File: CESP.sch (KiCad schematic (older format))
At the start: 5 parts

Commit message: First draft of schematic
First draft of having added and connected items in the schematic,
annotated and sized the devices and added a netlist.
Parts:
- removed U?: LTC1594CS, TSSOP14, symbol LTC1594CS
- removed U?: TL074, TSSOP14, symbol TL074
- removed U? (x3): TL074, symbol TL074
- added BT1, BT2: 9V, ~, symbol BATTERY
- added C1, C2, C5: .1µF, ~, symbol C
- added C3, C4: 10µF, ~, symbol CAPAPOL
- added R1: 68K, ~, symbol R
- added R2, R3, R5: 1K, ~, symbol R
- added R4: 10K, ~, symbol R
- added R6: 2K2, ~, symbol R
- added U1: 7555, ~, symbol 7555
- added U2: LM741, symbol LM741
- added U3: 7805, ~, symbol 7805
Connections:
- net labels added: +5V, +9V, -9V, GND
- wire segments 0 -> 47
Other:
- note removed: "NOTE: THIS IS JUST A TEST BOARD\nREMOVE ALL COMPONENTS AND CREATE YOUR OWN\nINCLUDE SCHEMATIC HOOKUPS/NETLIST"

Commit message: Post ERC...
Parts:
- removed BT1, BT2: 9V, ~, symbol BATTERY
- added K1: CONN_3, symbol CONN_3
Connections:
- net labels removed: +5V
- wire segments 47 -> 48
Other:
- moved on the sheet: C1, C2, C3, C4, C5, R1, R2, R3, R4, R5, R6, U1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

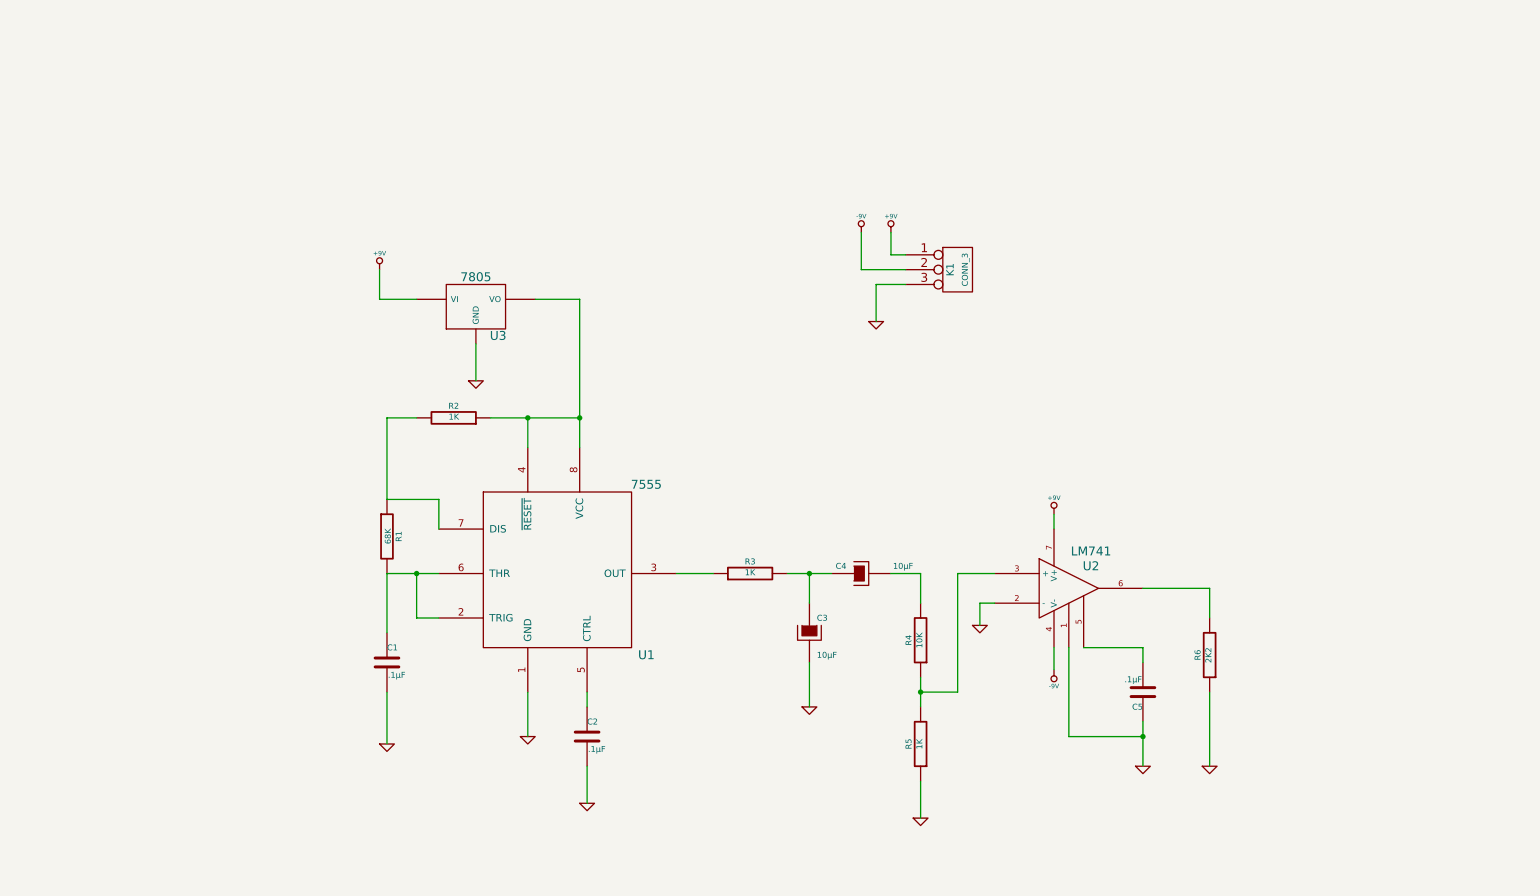
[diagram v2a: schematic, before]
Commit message: First draft of PCB layout
It's a total mess, but I got it to pass ERC, have the 7805 connected,
used a bunch of different foot prints, used vias and successfully beat
my head against the brickwall of KiCad.
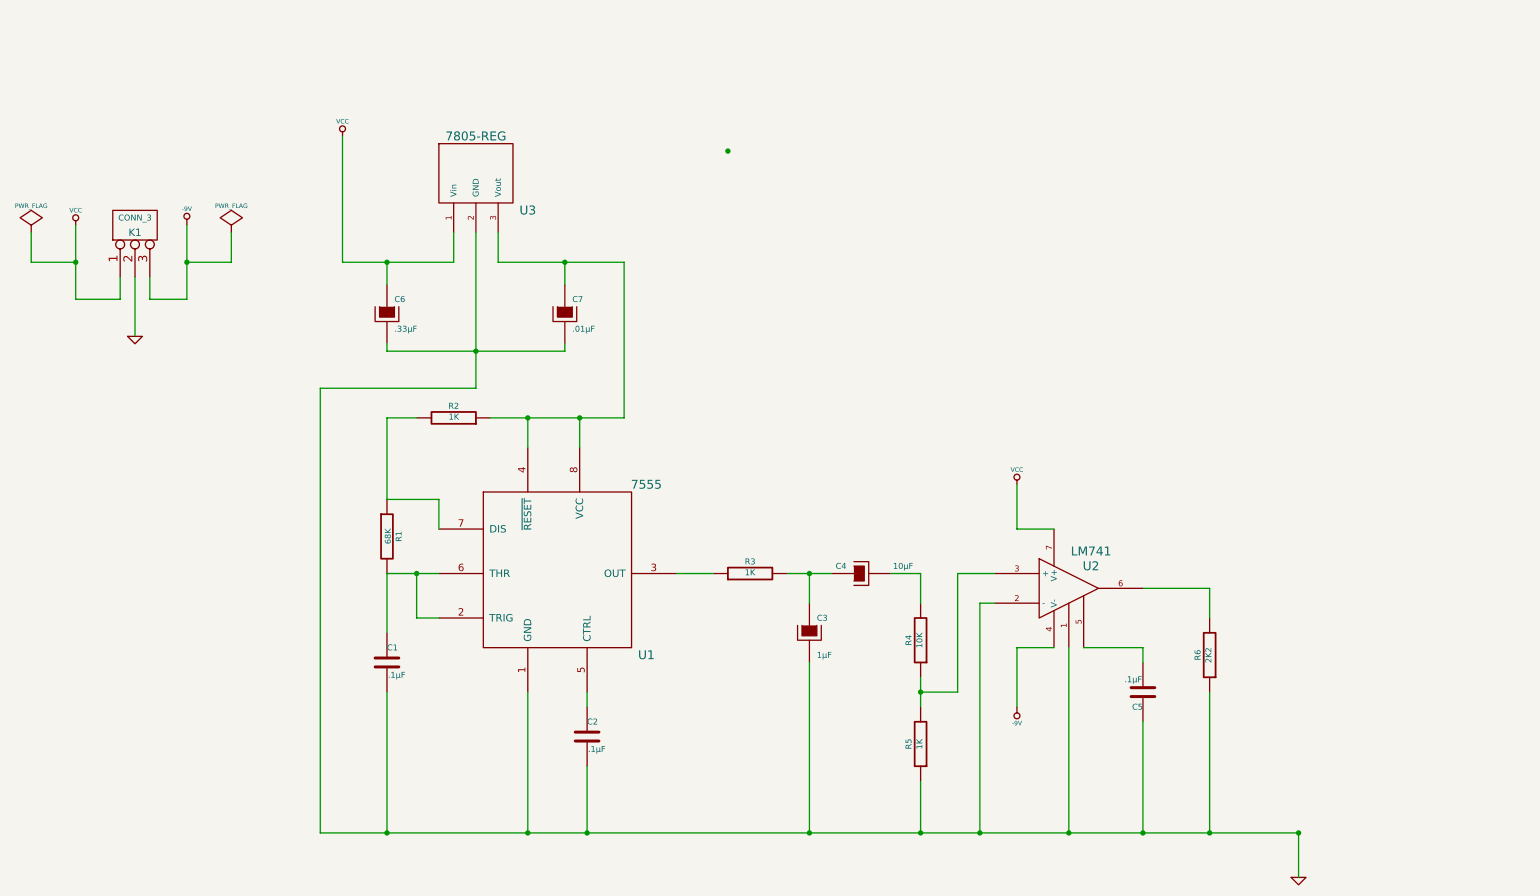
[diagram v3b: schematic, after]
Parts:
- removed U3: 7805, ~, symbol 7805
- added C6: .33µF, ~, symbol CAPAPOL
- added C7: .01µF, ~, symbol CAPAPOL
- added U3: 7805-REG, symbol 7805-REG
- C3: value 10µF -> 1µF
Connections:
- net -9V: now also K1.3 (P3); no longer K1.2 (PM)
- net GND: now also K1.2 (PM), C6.2, C7.2, U3.2 (GND); no longer K1.3 (P3)
- net at R2.1, U1.4 (~RESET), U1.8 (VCC): now also C7.1, U3.3 (Vout)
- net +9V renamed VCC
- net VCC: now also C6.1, U3.1 (Vin)
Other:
- moved on the sheet: K1

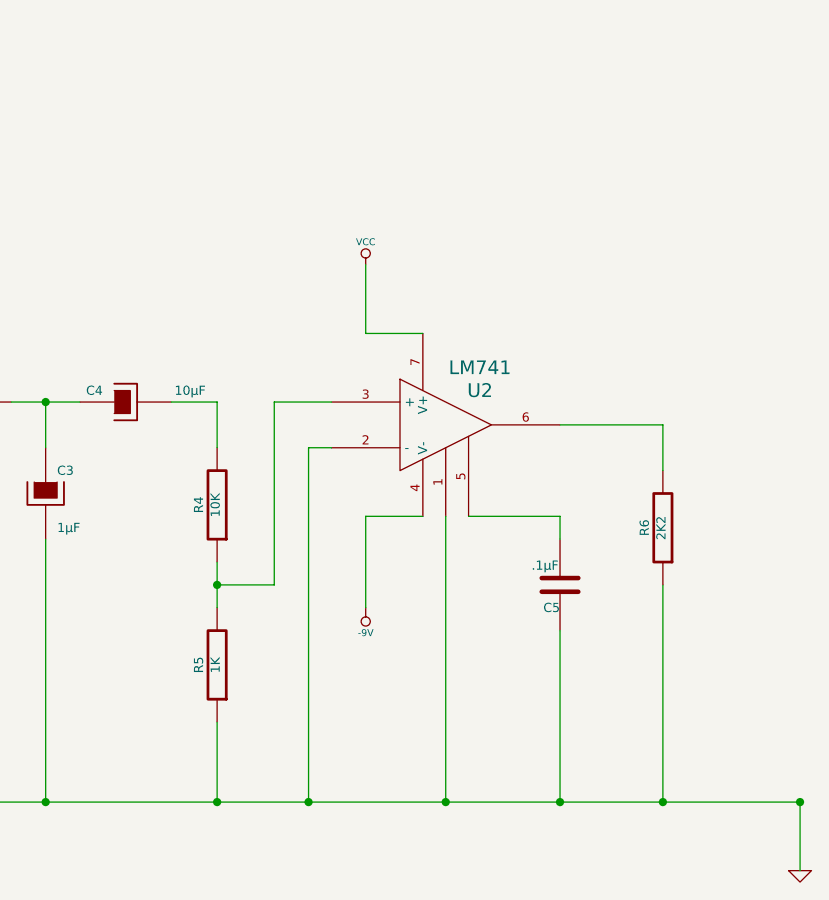
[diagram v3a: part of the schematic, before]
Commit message: Added headers and SPI vs SPI logo...
Headers added to allow customizing the Signal and Feedback resistors.

Headers added to allow measurement with an oscilloscope.

SPI vs. SPI logo from John Lohe added.
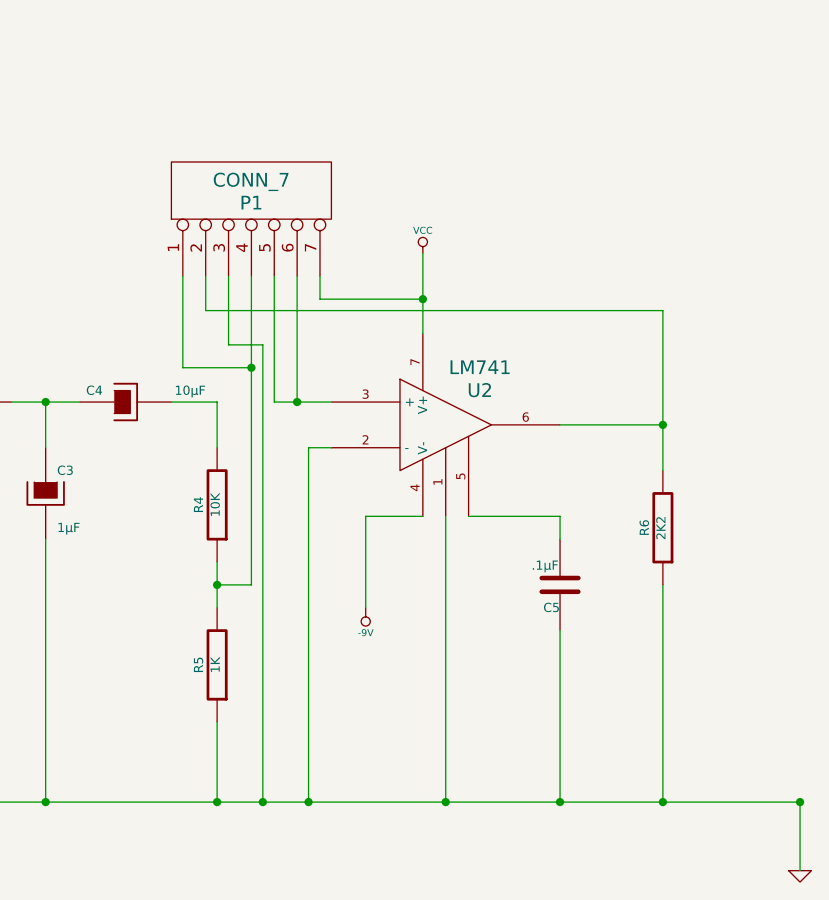
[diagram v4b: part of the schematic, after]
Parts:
- added P1: CONN_7, symbol CONN_7
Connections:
- net GND: now also P1.3 (P3)
- net VCC: now also P1.7 (P7)
- net at R4.1, R5.2: now also P1.1 (P1), P1.4 (P4); no longer U2.3 (+)
- net at R6.2, U2.6: now also P1.2 (P2)
- new net: P1.5 (P5), P1.6 (P6), U2.3 (+)
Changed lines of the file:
@@
 Sheet 1 1
 Title ""
-Date "27 jan 2014"
+Date "28 jan 2014"
 Rev ""
 Comp ""
@@
 Wire Wire Line
 	6800 5100 6800 5300
-Wire Wire Line
-	7300 4400 7050 4400
-Wire Wire Line
-	7050 4400 7050 5200
-Wire Wire Line
-	7050 5200 6800 5200
 Connection ~ 6800 5200
 Wire Wire Line
@@
 	8300 4500 8750 4500
 Wire Wire Line
-	8750 4500 8750 4700
+	8750 4000 8750 4700
 Wire Wire Line
 	4500 3350 4500 3550
@@
 Wire Wire Line
 	7300 4600 7200 4600
-Wire Wire Line
-	7200 4600 7200 6150
 Connection ~ 7200 6150
 $Comp
@@
 	9350 6150 9350 6450
 Wire Wire Line
-	7450 4100 7700 4100
-Wire Wire Line
-	7450 3800 7450 4100
-Wire Wire Line
 	7700 4900 7450 4900
 Wire Wire Line
 	7450 4900 7450 5300
 $Comp
-L VCC #PWR01
+L VCC #PWR1
 U 1 1 52E6ACAC
 P 1100 2050
-F 0 "#PWR01" H 1100 2150 30  0001 C CNN
+F 0 "#PWR1" H 1100 2150 30  0001 C CNN
 F 1 "VCC" H 1100 2150 30  0000 C CNN
 F 2 "" H 1100 2050 60  0000 C CNN
@@
 	1100 2550 1100 2050
 $Comp
-L -9V #PWR02
+L -9V #PWR3
 U 1 1 52E6AD0C
 P 1850 2050
-F 0 "#PWR02" H 1850 2020 20  0001 C CNN
+F 0 "#PWR3" H 1850 2020 20  0001 C CNN
 F 1 "-9V" H 1850 2160 30  0000 C CNN
 F 2 "~" H 1850 2050 60  0000 C CNN
@@
 	1600 2550 1600 2400
 $Comp
-L GND #PWR03
+L GND #PWR2
 U 1 1 52E6AD76
 P 1500 2800
-F 0 "#PWR03" H 1500 2800 30  0001 C CNN
+F 0 "#PWR2" H 1500 2800 30  0001 C CNN
 F 1 "GND" H 1500 2730 30  0001 C CNN
 F 2 "" H 1500 2800 60  0000 C CNN
@@
 	1500 2400 1500 2800
 $Comp
-L VCC #PWR04
+L VCC #PWR4
 U 1 1 52E6ADD6
 P 2900 1450
-F 0 "#PWR04" H 2900 1550 30  0001 C CNN
+F 0 "#PWR4" H 2900 1550 30  0001 C CNN
 F 1 "VCC" H 2900 1550 30  0000 C CNN
 F 2 "" H 2900 1450 60  0000 C CNN
@@
 $EndComp
 $Comp
-L GND #PWR05
+L GND #PWR7
 U 1 1 52E6AE37
 P 9350 6450
-F 0 "#PWR05" H 9350 6450 30  0001 C CNN
+F 0 "#PWR7" H 9350 6450 30  0001 C CNN
 F 1 "GND" H 9350 6380 30  0001 C CNN
 F 2 "" H 9350 6450 60  0000 C CNN
@@
 $EndComp
 $Comp
-L VCC #PWR06
+L VCC #PWR6
 U 1 1 52E6AE98
-P 7450 3800
-F 0 "#PWR06" H 7450 3900 30  0001 C CNN
-F 1 "VCC" H 7450 3900 30  0000 C CNN
-F 2 "" H 7450 3800 60  0000 C CNN
-F 3 "" H 7450 3800 60  0000 C CNN
-	1    7450 3800
-	1    0    0    -1
-$EndComp
-$Comp
-L -9V #PWR07
+P 7700 3750
+F 0 "#PWR6" H 7700 3850 30  0001 C CNN
+F 1 "VCC" H 7700 3850 30  0000 C CNN
+F 2 "" H 7700 3750 60  0000 C CNN
+F 3 "" H 7700 3750 60  0000 C CNN
+	1    7700 3750
+	1    0    0    -1
+$EndComp
+$Comp
+L -9V #PWR5
 U 1 1 52E6AF0B
 P 7450 5300
-F 0 "#PWR07" H 7450 5270 20  0001 C CNN
+F 0 "#PWR5" H 7450 5270 20  0001 C CNN
 F 1 "-9V" H 7450 5410 30  0000 C CNN
 F 2 "~" H 7450 5300 60  0000 C CNN
@@
 $EndComp
 $Comp
-L PWR_FLAG #FLG08
+L PWR_FLAG #FLG1
 U 1 1 52E6AFBB
 P 800 2100
-F 0 "#FLG08" H 800 2195 30  0001 C CNN
+F 0 "#FLG1" H 800 2195 30  0001 C CNN
 F 1 "PWR_FLAG" H 800 2280 30  0000 C CNN
 F 2 "" H 800 2100 60  0000 C CNN
@@
 $EndComp
 $Comp
-L PWR_FLAG #FLG09
+L PWR_FLAG #FLG2
 U 1 1 52E6B026
 P 2150 2100
-F 0 "#FLG09" H 2150 2195 30  0001 C CNN
+F 0 "#FLG2" H 2150 2195 30  0001 C CNN
 F 1 "PWR_FLAG" H 2150 2280 30  0000 C CNN
 F 2 "" H 2150 2100 60  0000 C CNN
@@
 	800  2300 1100 2300
 Connection ~ 1100 2300
+Wire Wire Line
+	7700 4100 7700 3750
+Connection ~ 7700 3950
+Wire Wire Line
+	7200 4600 7200 6150
+Wire Wire Line
+	6950 5200 6800 5200
+Wire Wire Line
+	7050 4400 7300 4400
+Connection ~ 7150 4400
+Wire Wire Line
+	7250 3950 7700 3950
+$Comp
+L CONN_7 P1
+U 1 1 52E70948
+P 6950 3500
+F 0 "P1" V 6920 3500 60  0000 C CNN
+F 1 "CONN_7" V 7020 3500 60  0000 C CNN
+F 2 "" H 6950 3500 60  0000 C CNN
+F 3 "" H 6950 3500 60  0000 C CNN
+	1    6950 3500
+	0    -1   -1   0
+$EndComp
+Wire Wire Line
+	6950 5200 6950 3850
+Wire Wire Line
+	7050 4400 7050 3850
+Wire Wire Line
+	7250 3950 7250 3850
+Wire Wire Line
+	7150 3850 7150 4400
+Wire Wire Line
+	6650 3850 6650 4250
+Wire Wire Line
+	6650 4250 6950 4250
+Connection ~ 6950 4250
+Wire Wire Line
+	6750 3850 6750 4000
+Wire Wire Line
+	6750 4000 8750 4000
+Connection ~ 8750 4500
+Wire Wire Line
+	6850 3850 6850 4150
+Wire Wire Line
+	6850 4150 7000 4150
+Wire Wire Line
+	7000 4150 7000 6150
+Connection ~ 7000 6150
 $EndSCHEMATC
